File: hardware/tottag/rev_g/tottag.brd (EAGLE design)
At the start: 68.1 x 39.6 mm, 200 parts, among them J1 USB4110-GF-A, J2 DM3AT-SF-PEJM5, J3 TC2030-JLINK-NL-2SIDE, J4 TC2030-JLINK-NL-2SIDE, J5 MOLEX-PICO-SPOX-3SIDE, Q1 CSD75207W15, Q4 CSD75207W15, T1 HHM1595A1, U1 DW1000, U10 STM32F091CC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

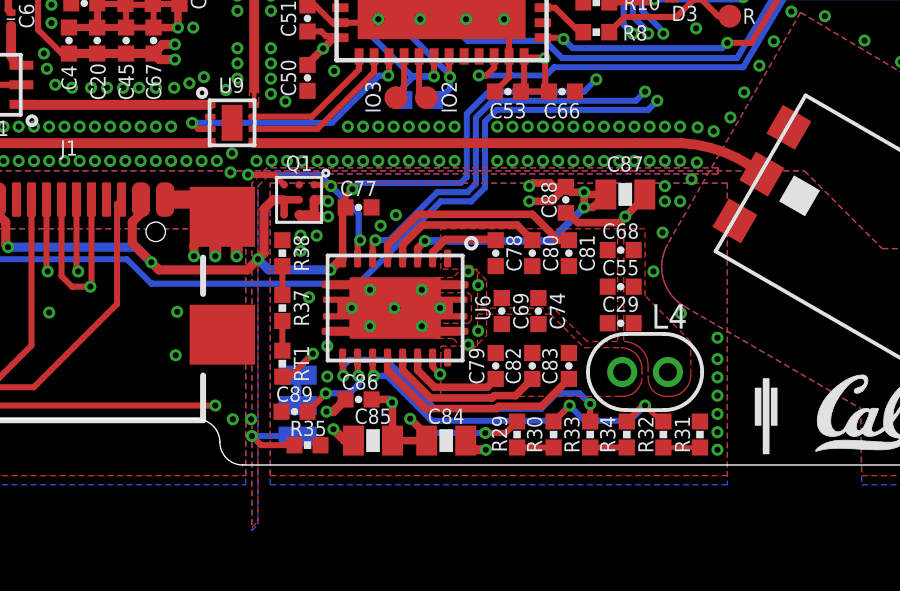
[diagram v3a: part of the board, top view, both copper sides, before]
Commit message: rev_g: more vias by caps of wireless charger
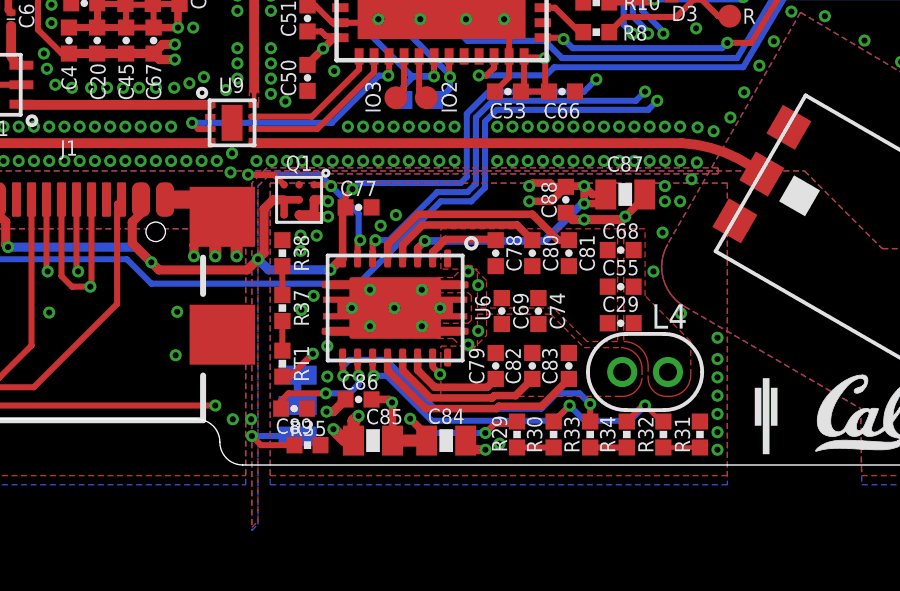
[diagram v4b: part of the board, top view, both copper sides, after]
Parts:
- moved C89 0.10 mm to (1.31, -4.57), turned to 0 degrees
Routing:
- net GND: track 168.2 -> 169.1 mm, vias 534 -> 538
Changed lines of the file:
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@@
 <attribute name="DIGIKEY" value="1253-CM105X5R106M25ATCT-ND" x="3.937" y="-5.6388" size="1.778" layer="27" rot="R180" display="off"/>
 <attribute name="MPN" value="CM105X5R106M25AT" x="3.937" y="-5.6388" size="1.778" layer="27" rot="R180" display="off"/>
-<attribute name="NAME" x="3.937" y="-5.08" size="0.508" layer="25" font="vector" ratio="18" align="bottom-center"/>
+<attribute name="NAME" x="4.318" y="-5.0927" size="0.508" layer="25" font="vector" ratio="18" align="bottom-center"/>
 </element>
 <element name="C86" library="passives" package="0402_CAP" value="0.1uF" x="3.4544" y="-4.2672" smashed="yes" rot="R180">
@@
 <attribute name="VALUE" x="-0.4826" y="-3.0734" size="0.508" layer="27" font="vector" ratio="18" rot="R270" align="bottom-center"/>
 </element>
-<element name="C89" library="passives" package="0402_CAP" value="0.1uF" x="1.3208" y="-4.6736" smashed="yes" rot="R180">
-<attribute name="DIGIKEY" value="490-6328-1-ND" x="1.3208" y="-4.6736" size="1.778" layer="27" rot="R180" display="off"/>
-<attribute name="MPN" value="GRM155R71C104KA88J " x="1.3208" y="-4.6736" size="1.778" layer="27" rot="R180" display="off"/>
-<attribute name="NAME" x="1.3208" y="-4.3434" size="0.508" layer="25" font="vector" ratio="18" align="bottom-center"/>
+<element name="C89" library="passives" package="0402_CAP" value="0.1uF" x="1.3081" y="-4.572" smashed="yes">
+<attribute name="DIGIKEY" value="490-6328-1-ND" x="1.3081" y="-4.572" size="1.778" layer="27" display="off"/>
+<attribute name="MPN" value="GRM155R71C104KA88J " x="1.3081" y="-4.572" size="1.778" layer="27" display="off"/>
+<attribute name="NAME" x="1.3081" y="-4.9022" size="0.508" layer="25" font="vector" ratio="18" rot="R180" align="bottom-center"/>
 </element>
 <element name="R37" library="passives" package="0402_RES" value="1k" x="0.9144" y="-1.2192" smashed="yes" rot="R270">
@@
 <via x="15.4178" y="-4.7498" extent="1-16" drill="0.2032"/>
 <via x="15.4178" y="-5.3594" extent="1-16" drill="0.2032"/>
-<via x="7.6962" y="-5.9436" extent="1-16" drill="0.2032"/>
+<via x="7.6835" y="-5.9436" extent="1-16" drill="0.2032"/>
 <via x="-0.127" y="-4.9276" extent="1-16" drill="0.2032"/>
 <via x="-14.351" y="-4.7244" extent="1-16" drill="0.2032"/>
@@
 <wire x1="5.728" y1="-1.9942" x2="5.5626" y2="-1.8288" width="0.3048" layer="1"/>
 <wire x1="3.287" y1="-5.6388" x2="2.9972" y2="-5.6388" width="0.3048" layer="1"/>
-<wire x1="2.9972" y1="-5.6388" x2="2.6162" y2="-5.2578" width="0.3048" layer="1"/>
+<wire x1="2.9972" y1="-5.6388" x2="2.6162" y2="-5.2578" width="0.4064" layer="1"/>
 <wire x1="2.3876" y1="-4.6736" x2="2.61493125" y2="-4.6736" width="0.3048" layer="1"/>
 <wire x1="2.61493125" y1="-4.6736" x2="3.02133125" y2="-4.2672" width="0.3048" layer="1"/>
-<wire x1="7.6962" y1="-5.9436" x2="7.3302" y2="-5.9436" width="0.3048" layer="1"/>
+<wire x1="7.6835" y1="-5.9436" x2="7.3302" y2="-5.9436" width="0.3048" layer="1"/>
 <wire x1="7.3302" y1="-5.9436" x2="7.0254" y2="-5.6388" width="0.3048" layer="1"/>
 <via x="13.6652" y="2.8448" extent="1-16" drill="0.2032"/>
@@
 <wire x1="-13.43850625" y1="25.804259375" x2="-13.037278125" y2="26.2054875" width="0.3048" layer="1"/>
 <wire x1="-13.01334375" y1="23.68134375" x2="-13.43850625" y2="24.10650625" width="0.3048" layer="1"/>
-<via x="1.8034" y="-0.8636" extent="1-16" drill="0.2032"/>
+<via x="1.9558" y="-0.8128" extent="1-16" drill="0.2032"/>
 <via x="2.413" y="-2.4892" extent="1-16" drill="0.2032"/>
 <via x="7.4422" y="-1.9812" extent="1-16" drill="0.2032"/>
@@
 </polygon>
 <wire x1="10.3632" y1="1.95453125" x2="10.44066875" y2="1.95453125" width="0.254" layer="1"/>
-<wire x1="10.44066875" y1="1.95453125" x2="10.7696" y2="1.6256" width="0.254" layer="1"/>
 <via x="12.3444" y="1.8288" extent="1-16" drill="0.2032"/>
-<wire x1="10.7696" y1="1.6256" x2="12.1412" y2="1.6256" width="0.254" layer="1"/>
-<wire x1="12.1412" y1="1.6256" x2="12.3444" y2="1.8288" width="0.254" layer="1"/>
 <wire x1="12.9944" y1="2.5654" x2="12.9944" y2="2.4788" width="0.254" layer="1"/>
 <wire x1="12.9944" y1="2.4788" x2="12.3444" y2="1.8288" width="0.254" layer="1"/>
@@
 <wire x1="-8.9004" y1="21.3106" x2="-8.1407" y2="20.5509" width="0.2032" layer="1"/>
 <wire x1="-8.1407" y1="20.5509" x2="-8.1407" y2="20.4851" width="0.2032" layer="1"/>
+<via x="8.1534" y="-5.7404" extent="1-16" drill="0.2032"/>
+<via x="3.4544" y="-4.8133" extent="1-16" drill="0.2032"/>
+<wire x1="3.4544" y1="-4.8133" x2="3.287" y2="-4.9807" width="0.4064" layer="1"/>
+<wire x1="3.287" y1="-4.9807" x2="3.287" y2="-5.6388" width="0.4064" layer="1"/>
+<via x="1.5494" y="-1.2827" extent="1-16" drill="0.2032"/>
+<wire x1="10.3632" y1="1.95453125" x2="10.5910625" y2="1.72666875" width="0.3048" layer="1"/>
+<wire x1="10.5910625" y1="1.72666875" x2="10.97333125" y2="1.72666875" width="0.3048" layer="1"/>
+<via x="10.97333125" y="1.72666875" extent="1-16" drill="0.2032"/>
+<wire x1="10.97333125" y1="1.72666875" x2="12.24226875" y2="1.72666875" width="0.3048" layer="1"/>
+<wire x1="12.24226875" y1="1.72666875" x2="12.3444" y2="1.8288" width="0.3048" layer="1"/>
 </signal>
 <signal name="VUSB">
@@
 <wire x1="5.4236" y1="0.7754" x2="5.6642" y2="1.016" width="0.254" layer="1"/>
 <via x="5.6642" y="1.016" extent="1-16" drill="0.2032"/>
-<wire x1="10.9728" y1="2.1336" x2="9.8552" y2="1.016" width="0.254" layer="16"/>
-<wire x1="5.6642" y1="1.016" x2="9.8552" y2="1.016" width="0.254" layer="16"/>
+<wire x1="10.9728" y1="2.2606" x2="10.8966" y2="2.2606" width="0.254" layer="16"/>
+<wire x1="10.8966" y1="2.2606" x2="9.652" y2="1.016" width="0.254" layer="16"/>
+<wire x1="5.6642" y1="1.016" x2="9.652" y2="1.016" width="0.254" layer="16"/>
 <polygon width="0.0508" layer="2">
 <vertex x="-16.2052" y="9.215759375"/>
@@
 <wire x1="-16.89226875" y1="15.92453125" x2="-16.6624" y2="16.1544" width="0.508" layer="1"/>
 <via x="-16.6624" y="16.1544" extent="1-16" drill="0.5"/>
-<via x="10.9728" y="2.1336" extent="1-16" drill="0.2032"/>
-<via x="10.9728" y="2.6416" extent="1-16" drill="0.2032"/>
-<wire x1="11.6944" y1="2.5654" x2="11.2626" y2="2.1336" width="0.254" layer="1"/>
-<wire x1="11.2626" y1="2.1336" x2="10.9728" y2="2.1336" width="0.254" layer="1"/>
-<wire x1="11.6944" y1="2.5654" x2="11.049" y2="2.5654" width="0.254" layer="1"/>
-<wire x1="11.049" y1="2.5654" x2="10.9728" y2="2.6416" width="0.254" layer="1"/>
-<wire x1="10.9728" y1="2.6416" x2="10.54226875" y2="2.6416" width="0.254" layer="1"/>
-<wire x1="10.54226875" y1="2.6416" x2="10.3632" y2="2.82066875" width="0.254" layer="1"/>
-<wire x1="10.9728" y1="2.6416" x2="10.9728" y2="2.1336" width="0.254" layer="1"/>
+<via x="10.9728" y="2.2606" extent="1-16" drill="0.2032"/>
+<via x="10.9728" y="2.8448" extent="1-16" drill="0.2032"/>
+<wire x1="11.6944" y1="2.5654" x2="11.3896" y2="2.2606" width="0.254" layer="1"/>
+<wire x1="11.3896" y1="2.2606" x2="10.9728" y2="2.2606" width="0.254" layer="1"/>
+<wire x1="11.6944" y1="2.5654" x2="11.2522" y2="2.5654" width="0.254" layer="1"/>
+<wire x1="11.2522" y1="2.5654" x2="10.9728" y2="2.8448" width="0.254" layer="1"/>
+<wire x1="10.3632" y1="2.82066875" x2="10.38733125" y2="2.8448" width="0.254" layer="1"/>
+<wire x1="10.9728" y1="2.8448" x2="10.38733125" y2="2.8448" width="0.254" layer="1"/>
+<wire x1="10.9728" y1="2.8448" x2="10.9728" y2="2.2606" width="0.254" layer="1"/>
 <wire x1="10.3632" y1="2.82066875" x2="9.98093125" y2="2.82066875" width="0.254" layer="1"/>
 <wire x1="9.98093125" y1="2.82066875" x2="9.8552" y2="2.9464" width="0.254" layer="1"/>
@@
 <wire x1="4.572" y1="-4.3688" x2="4.587" y2="-4.3838" width="0.254" layer="1"/>
 <wire x1="4.587" y1="-4.3838" x2="4.587" y2="-5.6388" width="0.254" layer="1"/>
-<wire x1="4.587" y1="-5.6388" x2="5.7254" y2="-5.6388" width="0.254" layer="1"/>
+<wire x1="4.587" y1="-5.6388" x2="5.7254" y2="-5.6388" width="0.4064" layer="1"/>
 <wire x1="5.7254" y1="-5.6388" x2="5.7254" y2="-5.4619375" width="0.254" layer="1"/>
 <wire x1="5.7254" y1="-5.4619375" x2="5.17363125" y2="-4.91016875" width="0.254" layer="1"/>
-<wire x1="7.6802" y1="-5.3848" x2="8.35533125" y2="-5.3848" width="0.2032" layer="1"/>
-<wire x1="8.35533125" y1="-5.3848" x2="8.7376" y2="-5.00253125" width="0.2032" layer="1"/>
+<wire x1="8.66013125" y1="-5.08" x2="7.985" y2="-5.08" width="0.2032" layer="1"/>
+<wire x1="7.6802" y1="-5.3848" x2="7.985" y2="-5.08" width="0.2032" layer="1"/>
+<wire x1="8.66013125" y1="-5.08" x2="8.7376" y2="-5.00253125" width="0.2032" layer="1"/>
 <wire x1="5.9236" y1="-2.8692" x2="5.9236" y2="-3.1804" width="0.2032" layer="1"/>
 <wire x1="5.9236" y1="-3.1804" x2="6.1722" y2="-3.429" width="0.2032" layer="1"/>
@@
 <wire x1="3.4544" y1="-3.7592" x2="3.1496" y2="-4.064" width="0.2032" layer="16"/>
 <via x="2.3622" y="-4.064" extent="1-16" drill="0.2032"/>
-<wire x1="2.3622" y1="-4.064" x2="1.75386875" y2="-4.67233125" width="0.2032" layer="1"/>
-<wire x1="1.75386875" y1="-4.67233125" x2="1.75386875" y2="-4.6736" width="0.2032" layer="1"/>
 <wire x1="3.1496" y1="-4.064" x2="2.3622" y2="-4.064" width="0.2032" layer="16"/>
 <wire x1="1.4224" y1="-4.4704" x2="1.9558" y2="-4.4704" width="0.2032" layer="16"/>
-<wire x1="1.9558" y1="-4.4704" x2="2.3622" y2="-4.064" width="0.2032" layer="16"/>
 <via x="15.589" y="17.5954" extent="1-16" drill="0.2032"/>
 <wire x1="15.589" y1="17.5954" x2="15.589" y2="17.7226" width="0.2032" layer="16"/>
@@
 <wire x1="6.19685625" y1="2.3368" x2="1.524" y2="-2.33605625" width="0.2032" layer="15"/>
 <wire x1="1.524" y1="-2.33605625" x2="1.524" y2="-3.2258" width="0.2032" layer="15"/>
+<wire x1="0.87503125" y1="-4.572" x2="0.87503125" y2="-4.30656875" width="0.2032" layer="1"/>
+<wire x1="0.87503125" y1="-4.30656875" x2="1.1176" y2="-4.064" width="0.2032" layer="1"/>
+<wire x1="1.1176" y1="-4.064" x2="2.3622" y2="-4.064" width="0.2032" layer="1"/>
+<wire x1="0.87503125" y1="-4.572" x2="1.4224" y2="-4.4704" width="0" layer="19" extent="1-16"/>
 </signal>
 <signal name="N$67">

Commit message: rev_g: remove 1% tol from value field
Several R's have tol requirements, but none of the others specify this way
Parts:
- R15: value 11k 1% -> 11k
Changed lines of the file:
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@@
 <attribute name="VALUE" x="-14.732" y="13.7922" size="0.508" layer="27" font="vector" ratio="18" rot="R180" align="bottom-center"/>
 </element>
-<element name="R15" library="passives" package="0402_RES" value="11k 1%" x="-15.3162" y="13.9192" smashed="yes" rot="R90">
+<element name="R15" library="passives" package="0402_RES" value="11k" x="-15.3162" y="13.9192" smashed="yes" rot="R90">
 <attribute name="NAME" x="-15.3416" y="14.6558" size="0.508" layer="25" font="vector" ratio="18" align="bottom-center"/>
 <attribute name="VALUE" x="-13.9192" y="13.9192" size="0.508" layer="27" font="vector" ratio="18" rot="R90" align="bottom-center"/>
